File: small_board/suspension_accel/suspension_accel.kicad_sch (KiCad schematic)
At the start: 10 parts, among them IC1 TJA1050T_CM,118, IC2 AMS1117-3.3, IC3 ESP32-S3-MINI-1-N8, J1 OSTTE040104

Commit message: small_board work, added buttons
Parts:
- added J2: BM04B-GVHS-TB_LF__SN_, BM04BGVHSTBLFSN, symbol BM04B-GVHS-TB_LF__SN_:BM04B-GVHS-TB_LF__SN_
- added R4: RR0816P-103-D, RESC1608X60N, symbol RR0816P-103-D:RR0816P-103-D
- added S1, S2: TL3301FF160QG, TL3301FF160QG, symbol TL3301FF160QG:TL3301FF160QG
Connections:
- net +3.3V: now also R4.2 (R2)
- net +5V: now also J2.4
- net GND: now also J2.1, S1.3, S2.2
- net at IC3.39 (TXD0): now also J2.3
- net at IC3.4 (IO0): now also S2.4
- net at IC3.40 (RXD0): now also J2.2
- net at IC3.45 (EN): now also R4.1 (R1), S1.1
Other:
- moved on the sheet: IC2, IC3

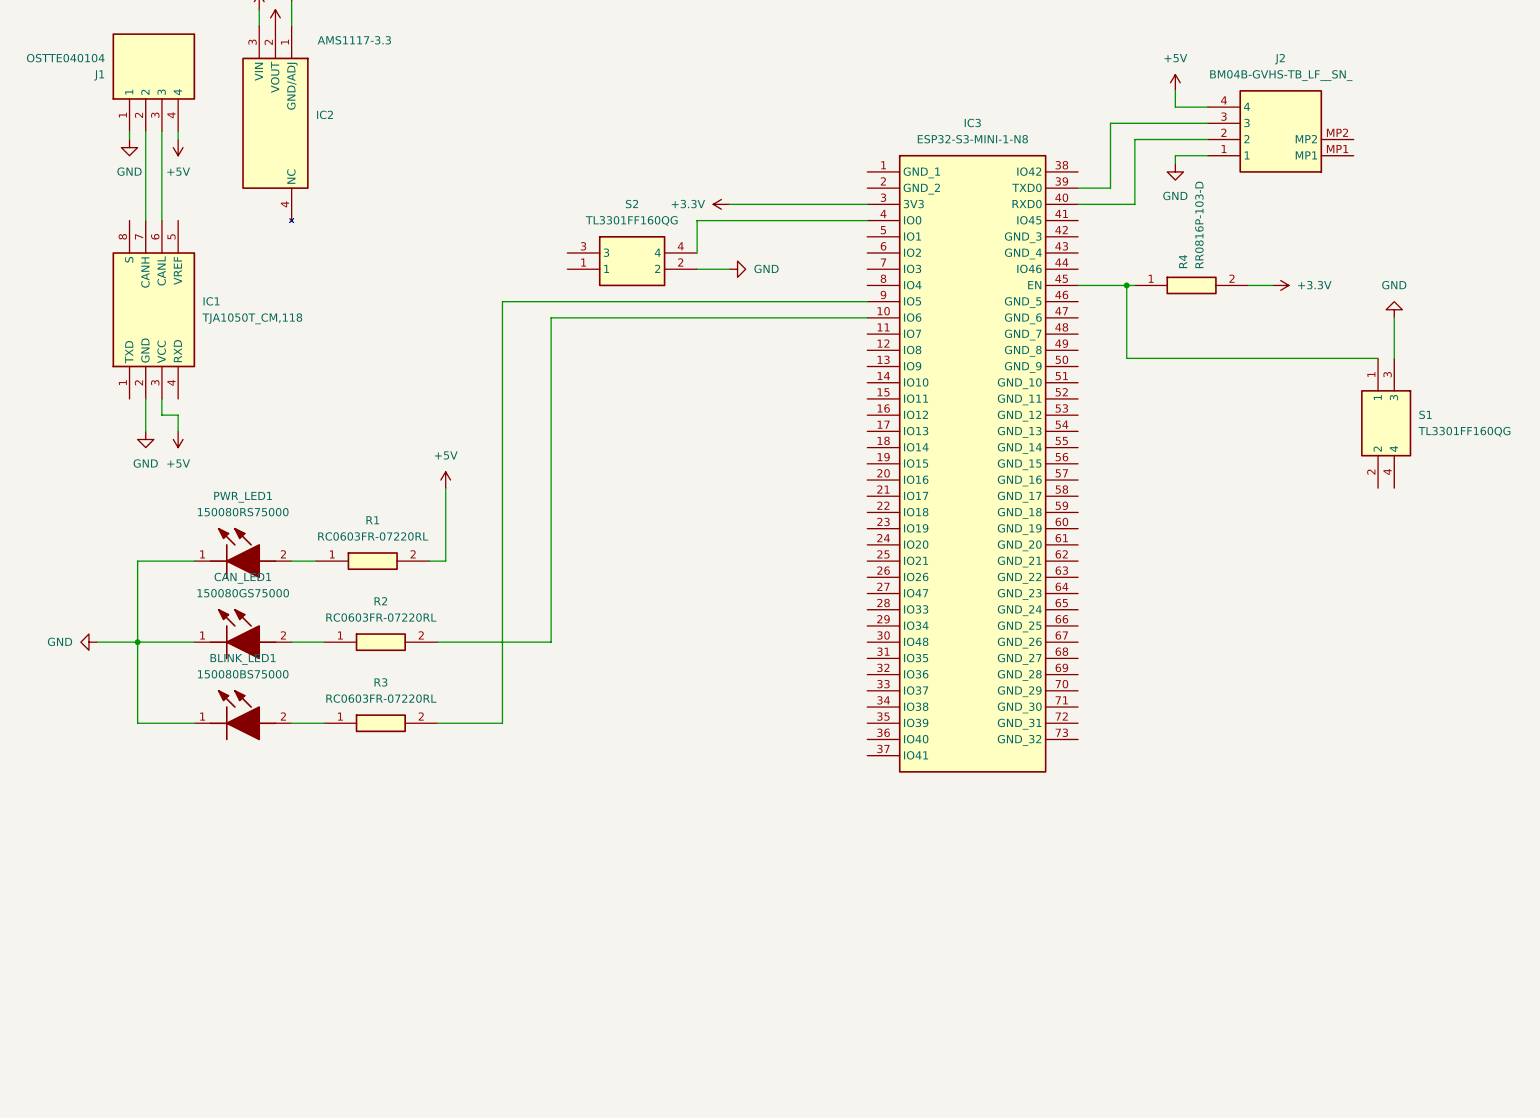
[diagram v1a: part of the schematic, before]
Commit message: added MPU, smaller buttons, started routing
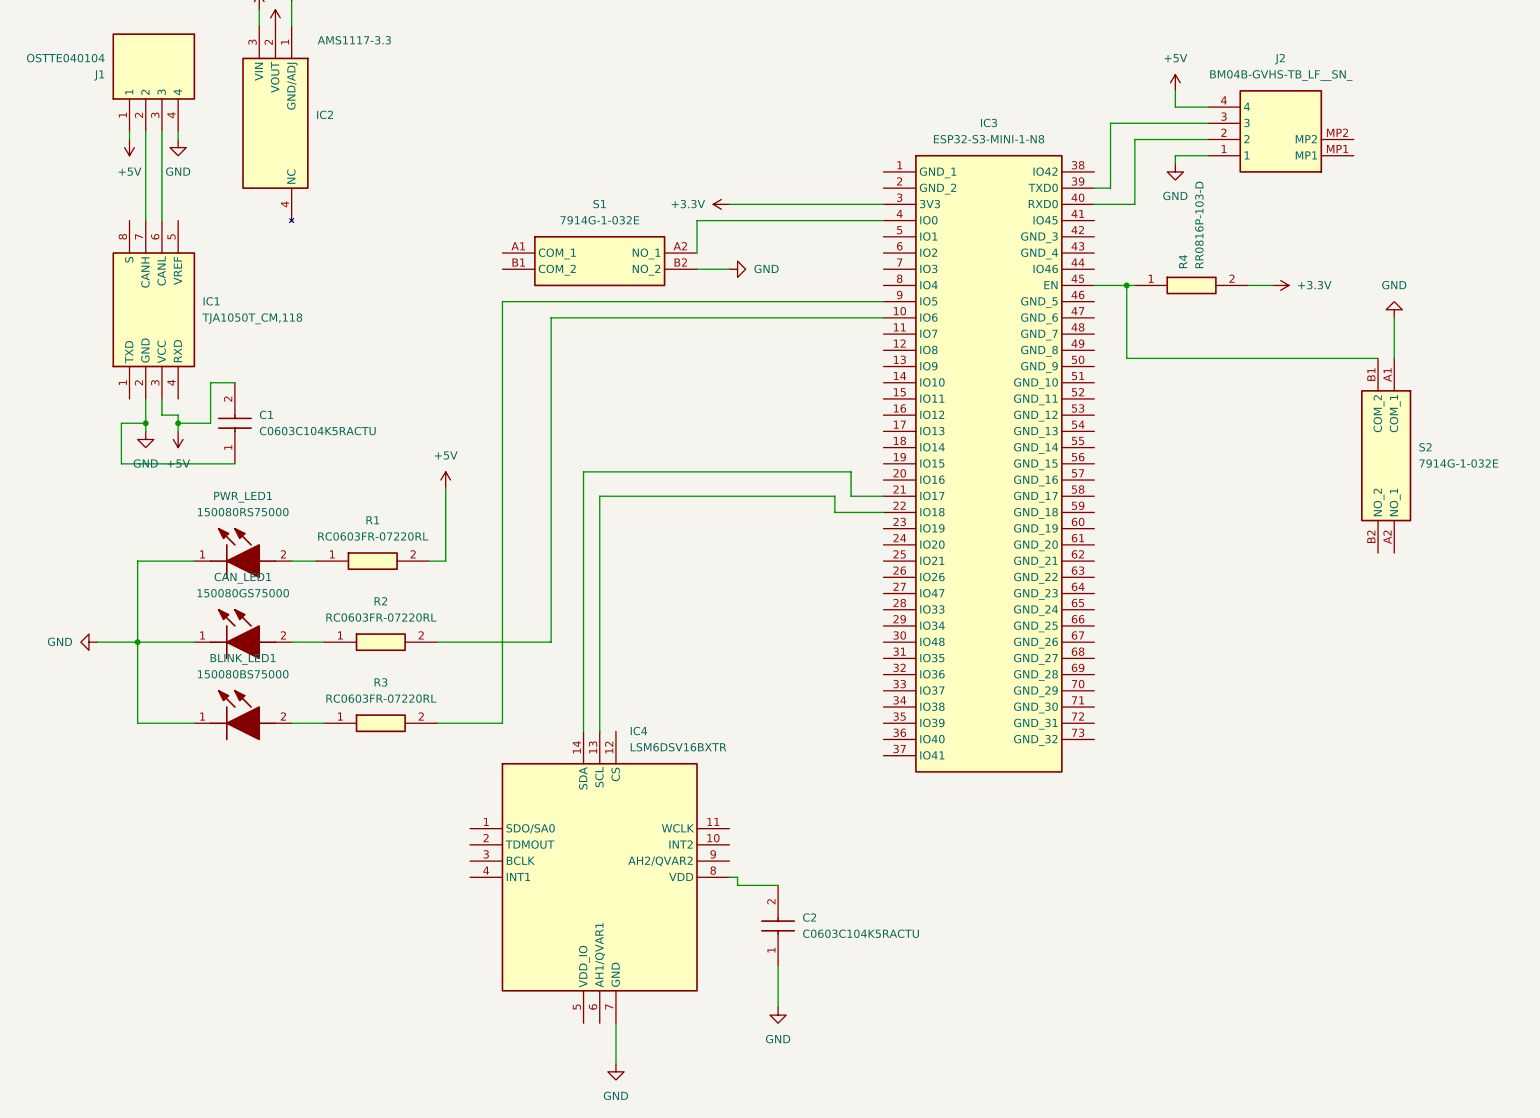
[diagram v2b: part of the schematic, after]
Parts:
- removed S1, S2: TL3301FF160QG, TL3301FF160QG, symbol TL3301FF160QG:TL3301FF160QG
- added C1, C2: C0603C104K5RACTU, C0603, symbol C0603C104K5RACTU:C0603C104K5RACTU
- added IC4: LSM6DSV16BXTR, LSM6DSV16BXTR, symbol LSM6DSV16BXTR:LSM6DSV16BXTR
- added S1, S2: 7914G-1-032E, 7914G1032E, symbol 7914G-1-032E:7914G-1-032E
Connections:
- net +5V: now also J1.1, C1.2; no longer J1.4
- net GND: now also J1.4, C1.1, C2.1, IC4.7 (GND), S1.B2 (NO_2), S2.A1 (COM_1); no longer J1.1
- net at IC3.4 (IO0): now also S1.A2 (NO_1)
- net at IC3.45 (EN), R4.1 (R1): now also S2.B1 (COM_2)
- net at IC3.21 (IO17): now also IC4.14 (SDA)
- net at IC3.22 (IO18): now also IC4.13 (SCL)
- new net: C2.2, IC4.8 (VDD)
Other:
- moved on the sheet: IC3

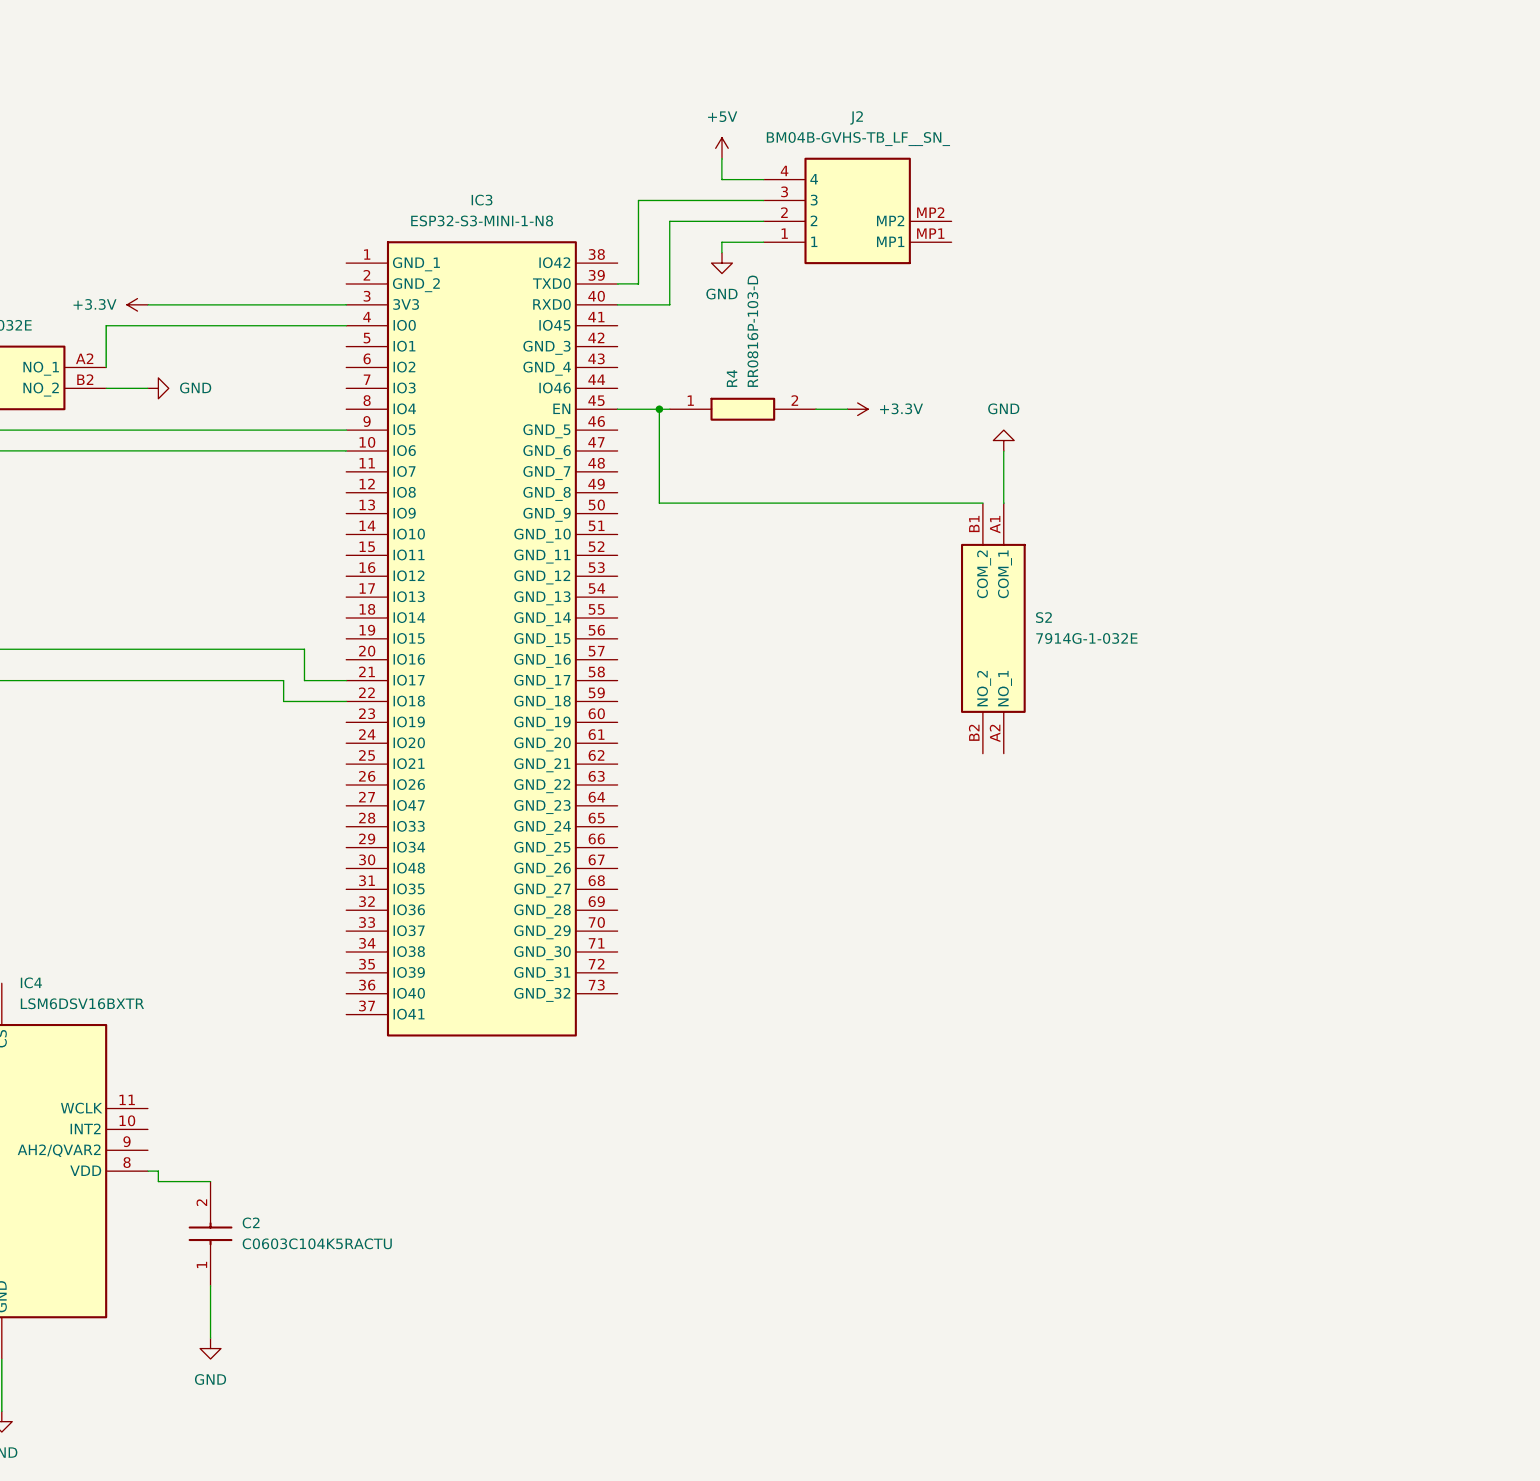
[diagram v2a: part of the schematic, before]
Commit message: added strain gauge adc, strain gauge ldo, comp components and headers for load cell hookups
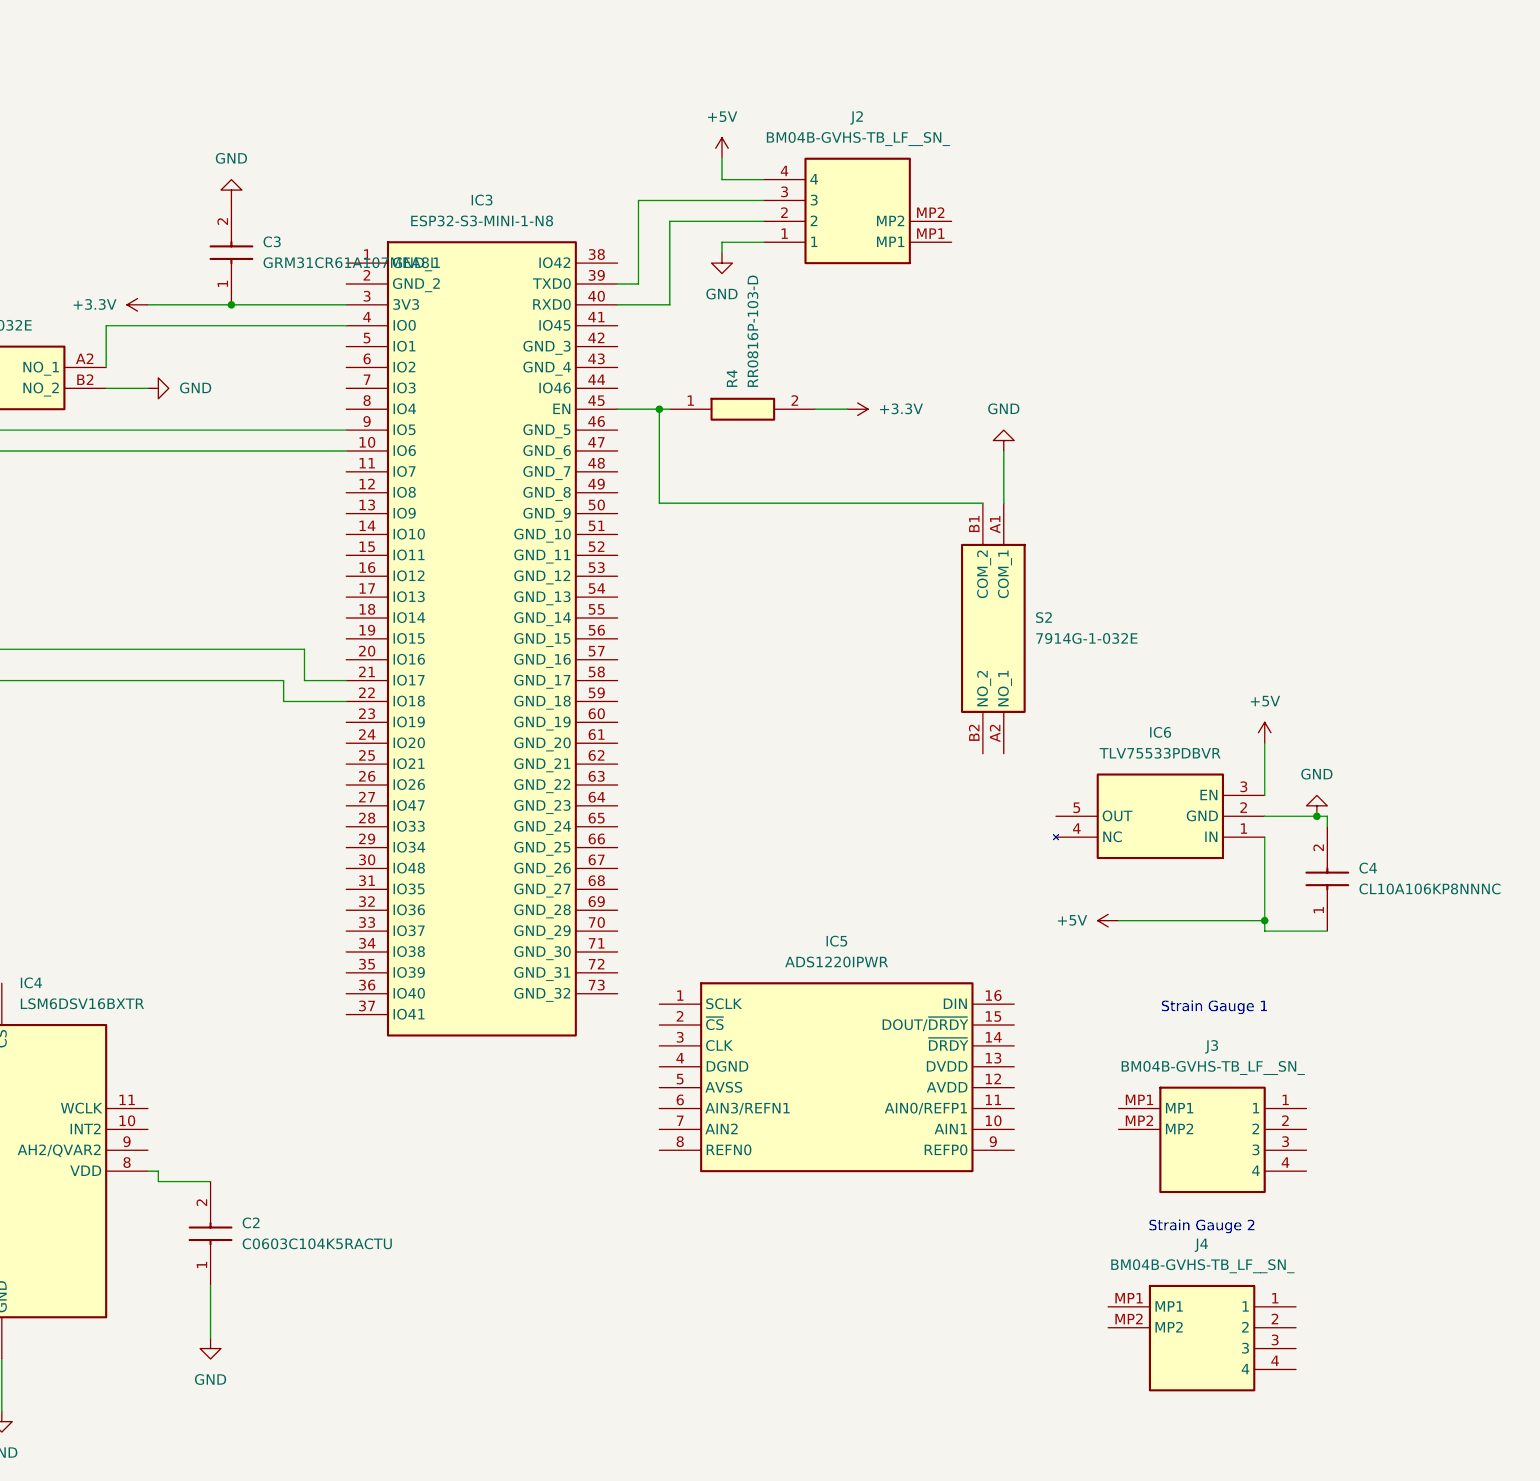
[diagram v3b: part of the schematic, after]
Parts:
- added C3: GRM31CR61A107MEA8L, GRM31x, symbol GRM31CR61A107MEA8L:GRM31CR61A107MEA8L
- added C4: CL10A106KP8NNNC, CAPC1608X90N, symbol CL10A106KP8NNNC:CL10A106KP8NNNC
- added IC5: ADS1220IPWR, SOP65P640X120-16N, symbol ADS1220IPWR:ADS1220IPWR
- added IC6: TLV75533PDBVR, SOT95P280X145-5N, symbol TLV75533PDBVR:TLV75533PDBVR
- added J3, J4: BM04B-GVHS-TB_LF__SN_, BM04BGVHSTBLFSN, symbol BM04B-GVHS-TB_LF__SN_:BM04B-GVHS-TB_LF__SN_
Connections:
- net +3.3V: now also C3.1
- net +5V: now also C4.1, IC6.1 (IN), IC6.3 (EN)
- net GND: now also C3.2, C4.2, IC6.2 (GND)
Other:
- note added: "Strain Gauge 1"
- note added: "Strain Gauge 2"
